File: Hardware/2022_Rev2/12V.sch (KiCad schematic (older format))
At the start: 18 parts

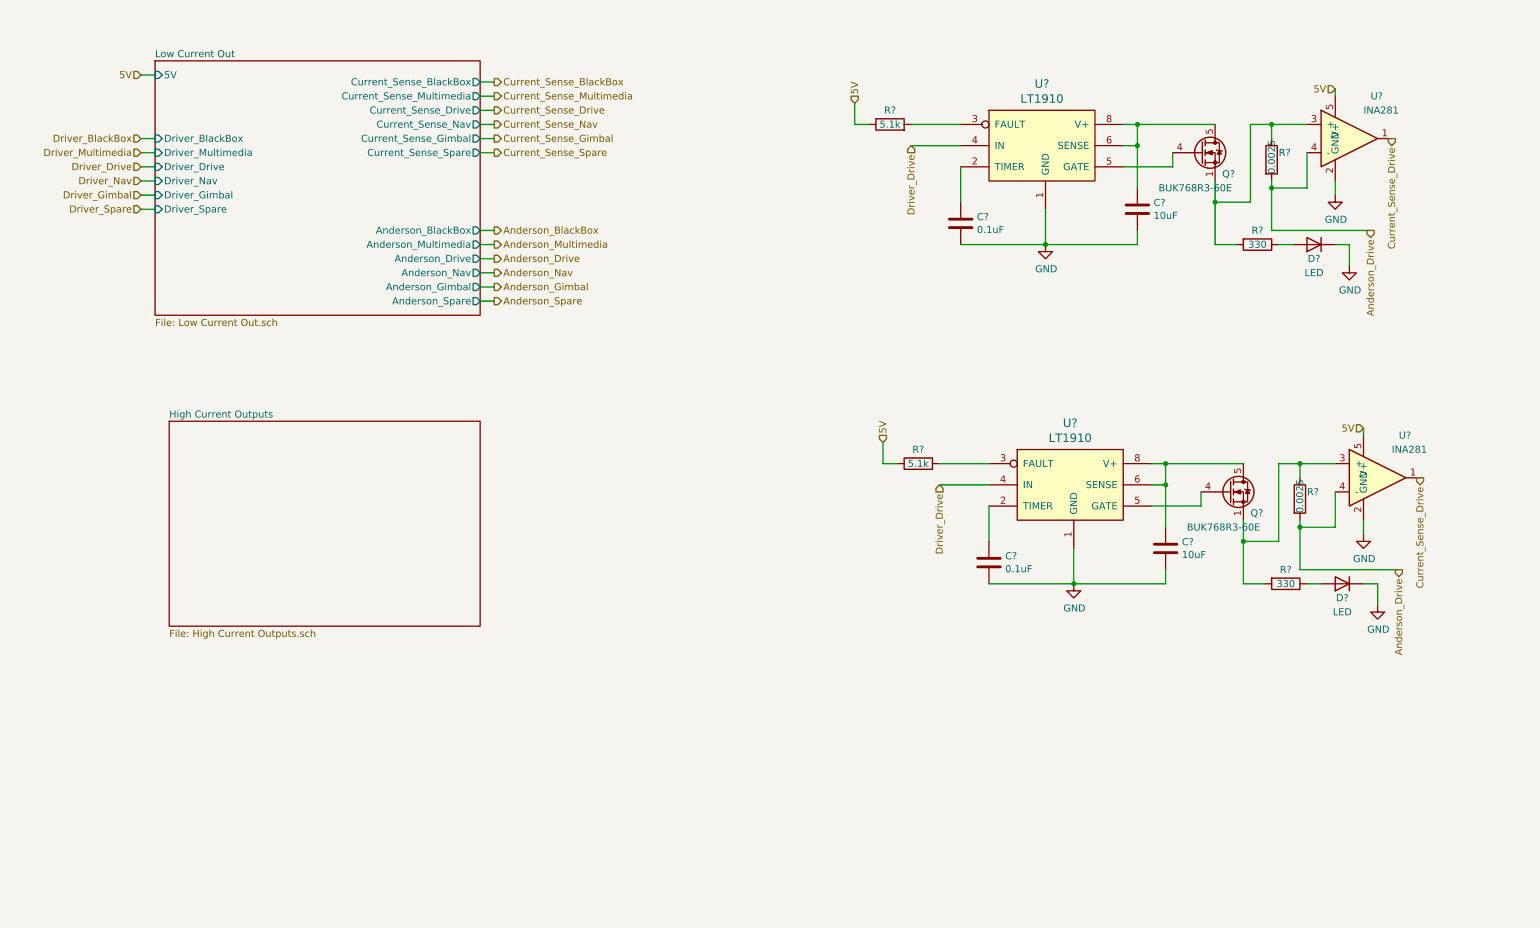
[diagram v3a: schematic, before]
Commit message: 12v switch circuits added
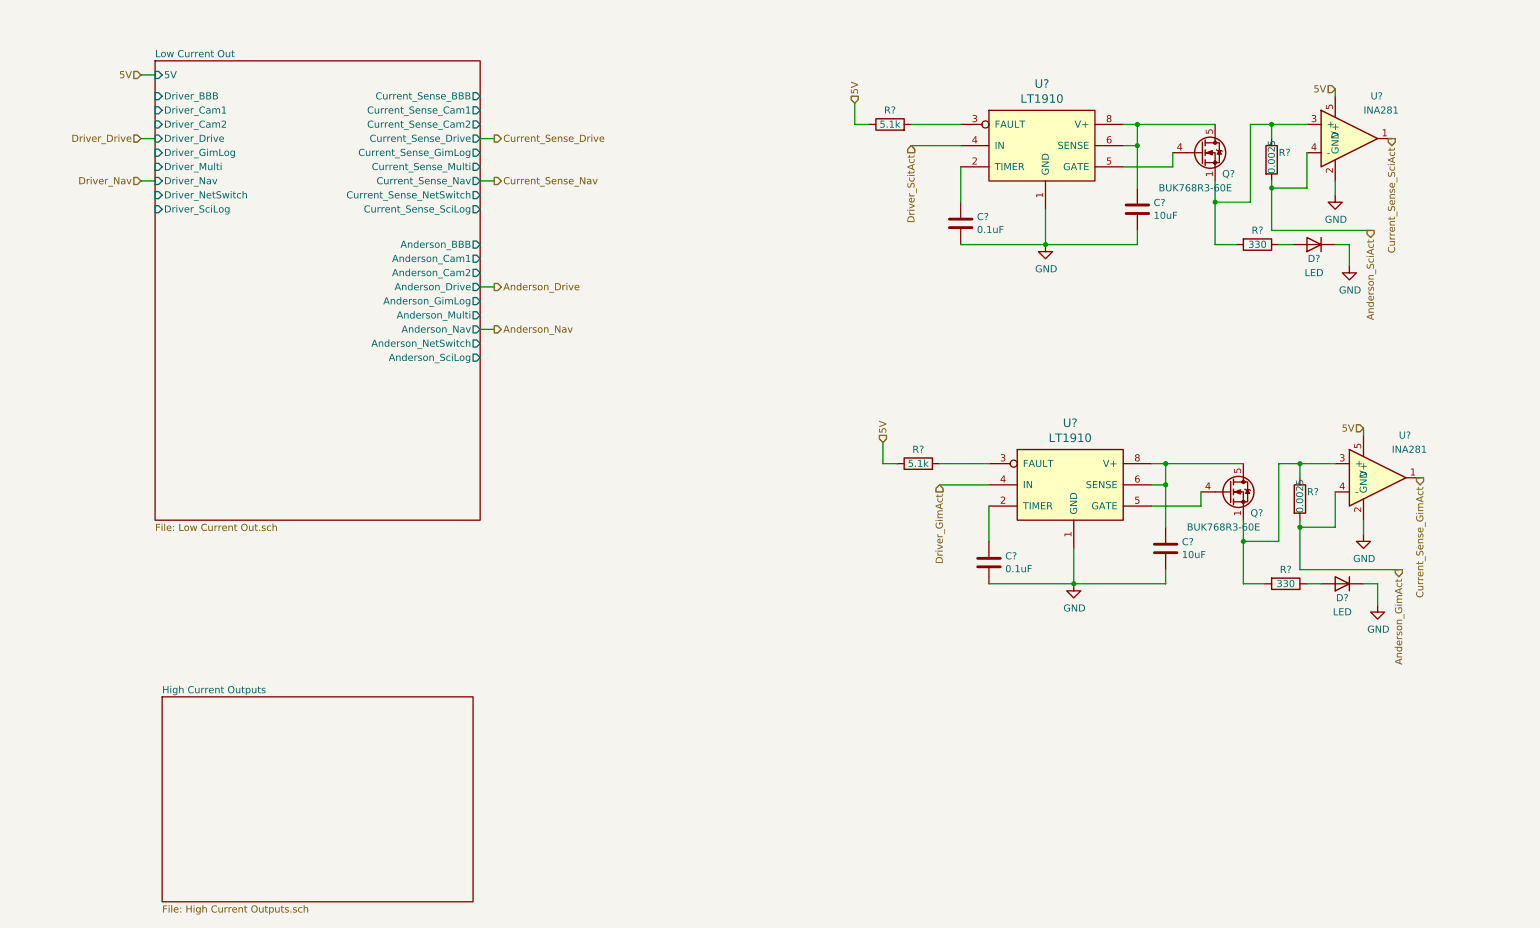
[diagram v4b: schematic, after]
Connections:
- net Anderson_Drive: no longer R?.2, R?.2, U?.4 (-), U?.4 (-)
- net Current_Sense_Drive: no longer U?.1, U?.1
- net Driver_Drive: no longer U?.4 (IN), U?.4 (IN)
- new net Anderson_GimAct: R?.2, U?.4 (-)
- new net Anderson_SciAct: R?.2, U?.4 (-)
- new net Current_Sense_GimAct: U?.1
- new net Current_Sense_SciAct: U?.1
- new net Driver_GimAct: U?.4 (IN)
- new net Driver_ScitAct: U?.4 (IN)
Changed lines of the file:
@@
 Comment4 ""
 $EndDescr
-$Sheet
-S 1450 900  2300 1800
-U 621219B0
-F0 "Low Current Out" 50
-F1 "Low Current Out.sch" 50
-F2 "Current_Sense_BlackBox" O R 3750 1050 50
-F3 "Anderson_BlackBox" O R 3750 2100 50
-F4 "Driver_BlackBox" I L 1450 1450 50
-F5 "5V" I L 1450 1000 50
-F6 "Current_Sense_Multimedia" O R 3750 1150 50
-F7 "Anderson_Multimedia" O R 3750 2200 50
-F8 "Driver_Multimedia" I L 1450 1550 50
-F9 "Current_Sense_Drive" O R 3750 1250 50
-F10 "Anderson_Drive" O R 3750 2300 50
-F11 "Driver_Drive" I L 1450 1650 50
-F12 "Current_Sense_Nav" O R 3750 1350 50
-F13 "Anderson_Nav" O R 3750 2400 50
-F14 "Driver_Nav" I L 1450 1750 50
-F15 "Current_Sense_Gimbal" O R 3750 1450 50
-F16 "Anderson_Gimbal" O R 3750 2500 50
-F17 "Driver_Gimbal" I L 1450 1850 50
-F18 "Current_Sense_Spare" O R 3750 1550 50
-F19 "Anderson_Spare" O R 3750 2600 50
-F20 "Driver_Spare" I L 1450 1950 50
-$EndSheet
 Text HLabel 1350 1000 0    50   Input ~ 0
 5V
 Text HLabel 1350 1450 0    50   Input ~ 0
-Driver_BlackBox
-Text HLabel 1350 1550 0    50   Input ~ 0
-Driver_Multimedia
-Text HLabel 1350 1650 0    50   Input ~ 0
 Driver_Drive
 Text HLabel 1350 1750 0    50   Input ~ 0
 Driver_Nav
-Text HLabel 1350 1850 0    50   Input ~ 0
-Driver_Gimbal
-Text HLabel 1350 1950 0    50   Input ~ 0
-Driver_Spare
 Wire Wire Line
 	1350 1000 1450 1000
@@
 	1350 1450 1450 1450
 Wire Wire Line
-	1450 1550 1350 1550
-Wire Wire Line
-	1350 1650 1450 1650
-Wire Wire Line
 	1450 1750 1350 1750
-Wire Wire Line
-	1350 1850 1450 1850
-Wire Wire Line
-	1450 1950 1350 1950
-Text HLabel 3850 1050 2    50   Output ~ 0
-Current_Sense_BlackBox
-Text HLabel 3850 1150 2    50   Output ~ 0
-Current_Sense_Multimedia
-Text HLabel 3850 1250 2    50   Output ~ 0
+Text HLabel 3850 1450 2    50   Output ~ 0
 Current_Sense_Drive
-Text HLabel 3850 1350 2    50   Output ~ 0
+Text HLabel 3850 1750 2    50   Output ~ 0
 Current_Sense_Nav
-Text HLabel 3850 1450 2    50   Output ~ 0
-Current_Sense_Gimbal
-Text HLabel 3850 1550 2    50   Output ~ 0
-Current_Sense_Spare
-Wire Wire Line
-	3850 1550 3750 1550
+Wire Wire Line
+	3850 1750 3750 1750
 Wire Wire Line
 	3750 1450 3850 1450
-Wire Wire Line
-	3850 1350 3750 1350
-Wire Wire Line
-	3750 1250 3850 1250
-Wire Wire Line
-	3850 1150 3750 1150
-Wire Wire Line
-	3750 1050 3850 1050
-Text HLabel 3850 2100 2    50   Output ~ 0
-Anderson_BlackBox
-Text HLabel 3850 2200 2    50   Output ~ 0
-Anderson_Multimedia
-Text HLabel 3850 2300 2    50   Output ~ 0
+Text HLabel 3850 2500 2    50   Output ~ 0
 Anderson_Drive
-Text HLabel 3850 2400 2    50   Output ~ 0
+Text HLabel 3850 2800 2    50   Output ~ 0
 Anderson_Nav
-Text HLabel 3850 2500 2    50   Output ~ 0
-Anderson_Gimbal
-Text HLabel 3850 2600 2    50   Output ~ 0
-Anderson_Spare
-Wire Wire Line
-	3850 2100 3750 2100
-Wire Wire Line
-	3750 2200 3850 2200
-Wire Wire Line
-	3850 2300 3750 2300
-Wire Wire Line
-	3750 2400 3850 2400
 Wire Wire Line
 	3850 2500 3750 2500
 Wire Wire Line
-	3750 2600 3850 2600
+	3750 2800 3850 2800
 $Sheet
-S 1550 3450 2200 1450
+S 1500 5400 2200 1450
 U 622EFCD1
 F0 "High Current Outputs" 50
@@
 	10000 3550 10000 3500
 Text HLabel 10400 3850 3    50   Output ~ 0
-Current_Sense_Drive
+Current_Sense_GimAct
 Text HLabel 10250 4500 3    50   Output ~ 0
-Anderson_Drive
+Anderson_GimAct
 Wire Wire Line
 	9550 4500 10250 4500
@@
 	6600 3750 6600 3600
 Text HLabel 7000 3900 3    50   Input ~ 0
-Driver_Drive
+Driver_GimAct
 Text HLabel 6600 3600 1    50   Input ~ 0
 5V
@@
 	9800 1150 9800 1100
 Text HLabel 10200 1450 3    50   Output ~ 0
-Current_Sense_Drive
+Current_Sense_SciAct
 Text HLabel 10050 2100 3    50   Output ~ 0
-Anderson_Drive
+Anderson_SciAct
 Wire Wire Line
 	9350 2100 10050 2100
@@
 	6400 1350 6400 1200
 Text HLabel 6800 1500 3    50   Input ~ 0
-Driver_Drive
+Driver_ScitAct
 Text HLabel 6400 1200 1    50   Input ~ 0
 5V
 Text HLabel 9800 1100 0    50   Input ~ 0
 5V
+$Sheet
+S 1450 900  2300 3250
+U 621219B0
+F0 "Low Current Out" 50
+F1 "Low Current Out.sch" 50
+F2 "5V" I L 1450 1000 50
+F3 "Current_Sense_Drive" O R 3750 1450 50
+F4 "Anderson_Drive" O R 3750 2500 50
+F5 "Driver_Drive" I L 1450 1450 50
+F6 "Current_Sense_Nav" O R 3750 1750 50
+F7 "Anderson_Nav" O R 3750 2800 50
+F8 "Driver_Nav" I L 1450 1750 50
+F9 "Current_Sense_BBB" O R 3750 1150 50
+F10 "Anderson_BBB" O R 3750 2200 50
+F11 "Current_Sense_Multi" O R 3750 1650 50
+F12 "Anderson_Multi" O R 3750 2700 50
+F13 "Current_Sense_Cam1" O R 3750 1250 50
+F14 "Anderson_Cam1" O R 3750 2300 50
+F15 "Driver_Cam1" I L 1450 1250 50
+F16 "Current_Sense_NetSwitch" O R 3750 1850 50
+F17 "Anderson_NetSwitch" O R 3750 2900 50
+F18 "Current_Sense_Cam2" O R 3750 1350 50
+F19 "Anderson_Cam2" O R 3750 2400 50
+F20 "Driver_Cam2" I L 1450 1350 50
+F21 "Driver_BBB" I L 1450 1150 50
+F22 "Driver_Multi" I L 1450 1650 50
+F23 "Current_Sense_GimLog" O R 3750 1550 50
+F24 "Anderson_GimLog" O R 3750 2600 50
+F25 "Driver_GimLog" I L 1450 1550 50
+F26 "Driver_NetSwitch" I L 1450 1850 50
+F27 "Current_Sense_SciLog" O R 3750 1950 50
+F28 "Anderson_SciLog" O R 3750 3000 50
+F29 "Driver_SciLog" I L 1450 1950 50
+$EndSheet
 $EndSCHEMATC

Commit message: teensy pins are done (I think)
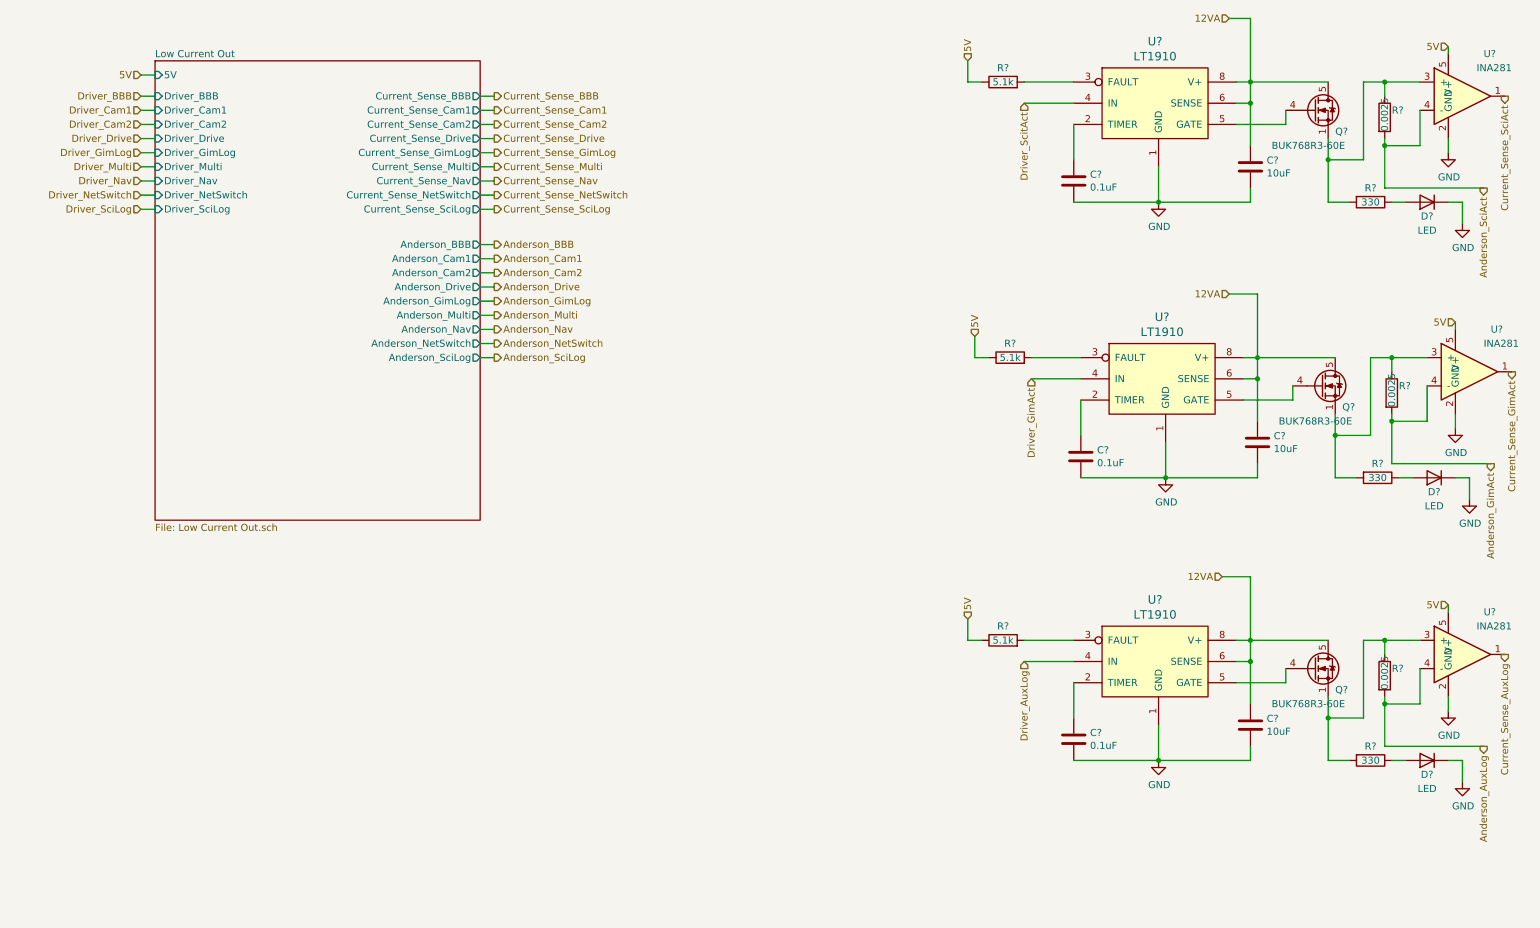
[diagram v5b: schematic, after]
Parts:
- added C?: 0.1uF, symbol Device:C
- added C?: 10uF, symbol Device:C
- added D?: LED, symbol Device:D
- added Q?: BUK768R3-60E, Package_TO_SOT_SMD:LFPAK33, symbol Transistor_FET:BUK7M9R9-60EX
- added R?: 5.1k, symbol Device:R
- added R?: 330, symbol Device:R
- added R?: 0.0025, symbol Device:R
- added U?: LT1910, symbol 2022_Rev2-rescue:LT1910-MRDT_ICs
- added U?: INA281, Package_TO_SOT_SMD:SOT-23-5, symbol 2022_Rev2-rescue:INA281-MRDT_ICs
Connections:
- net 5V: now also R?.1, U?.5 (V+)
- net GND: now also C?.2, C?.2, D?.1 (K), U?.1 (GND), U?.2 (GND)
- net 12VA: now reaches C?.1, Q?.5 (D), U?.6 (SENSE), U?.8 (V+)
- net 12VA: now also C?.1, Q?.5 (D), U?.6 (SENSE), U?.8 (V+), C?.1, Q?.5 (D), U?.6 (SENSE), U?.8 (V+)
- new net: R?.2, U?.3 (FAULT)
- new net: C?.1, U?.2 (TIMER)
- new net: Q?.4 (G), U?.5 (GATE)
- new net: Q?.1 (S), Q?.2 (S), Q?.3 (S), R?.1, R?.2, U?.3 (+)
- new net: D?.2 (A), R?.1
- new net Anderson_AuxLog: R?.2, U?.4 (-)
- new net Current_Sense_AuxLog: U?.1
- new net Driver_AuxLog: U?.4 (IN)
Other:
- moved on the sheet: C?, D?, Q?, R?, U?

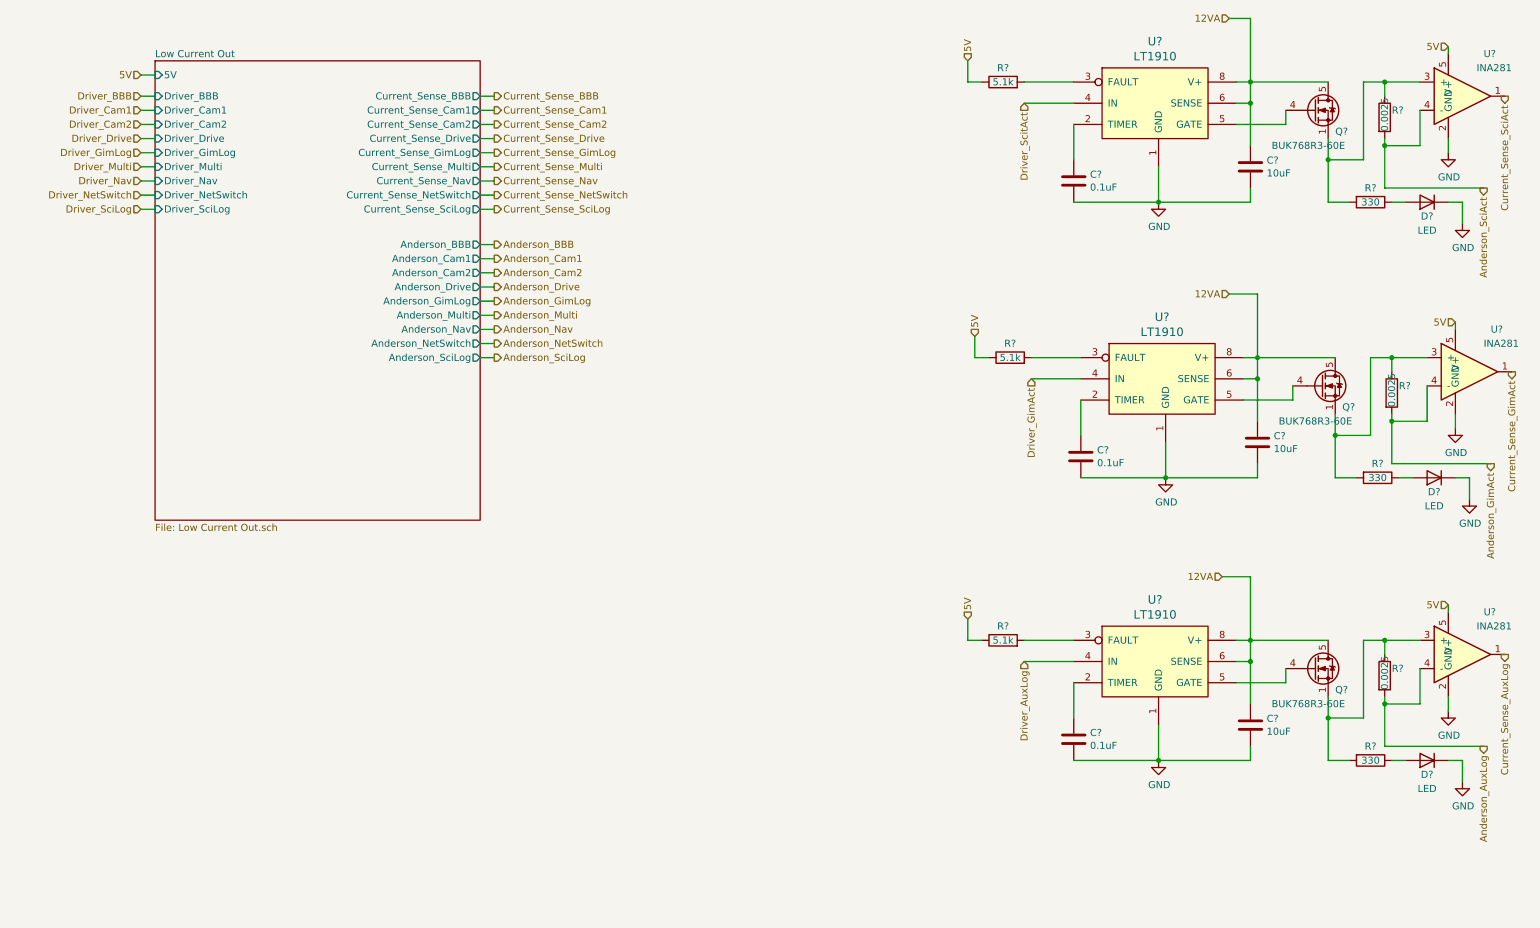
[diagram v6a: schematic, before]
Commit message: removed scilog/sciact
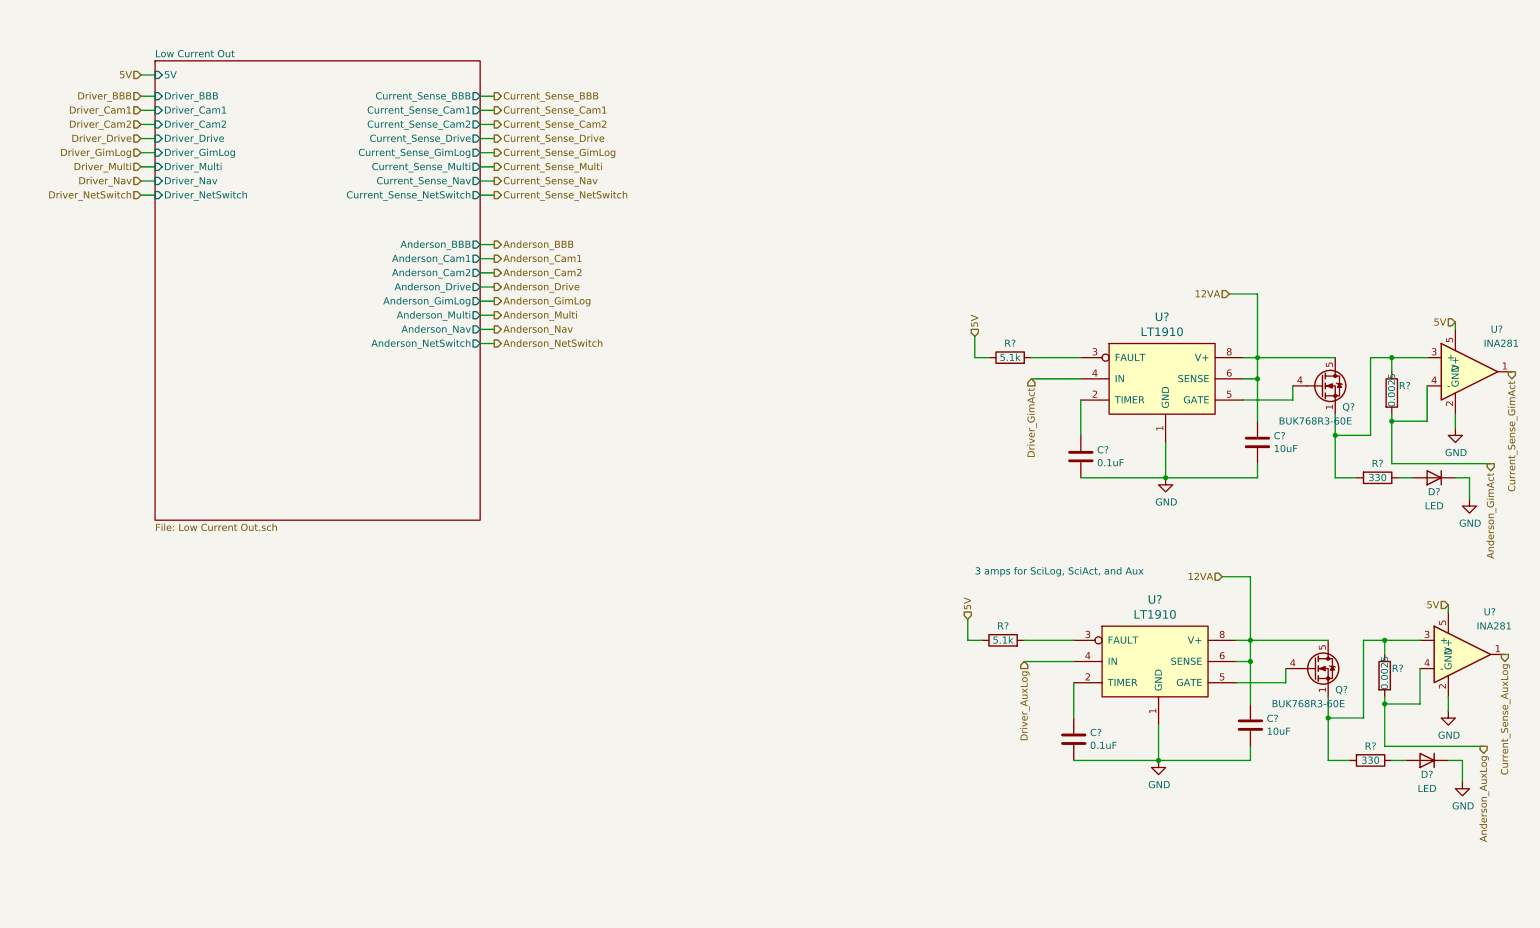
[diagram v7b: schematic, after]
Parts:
- removed C?: 0.1uF, symbol Device:C
- removed C?: 10uF, symbol Device:C
- removed D?: LED, symbol Device:D
- removed Q?: BUK768R3-60E, Package_TO_SOT_SMD:LFPAK33, symbol Transistor_FET:BUK7M9R9-60EX
- removed R?: 5.1k, symbol Device:R
- removed R?: 330, symbol Device:R
- removed R?: 0.0025, symbol Device:R
- removed U?: LT1910, symbol 2022_Rev2-rescue:LT1910-MRDT_ICs
- removed U?: INA281, Package_TO_SOT_SMD:SOT-23-5, symbol 2022_Rev2-rescue:INA281-MRDT_ICs
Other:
- note added: "3 amps for SciLog, SciAct, and Aux"
